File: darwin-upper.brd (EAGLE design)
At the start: 96 x 62 mm, 50 parts, among them U1 TC58CVG1S3HRAIG, U2 TC58CVG1S3HRAIG, U3 TC58CVG1S3HRAIG, U4 TC58CVG1S3HRAIG

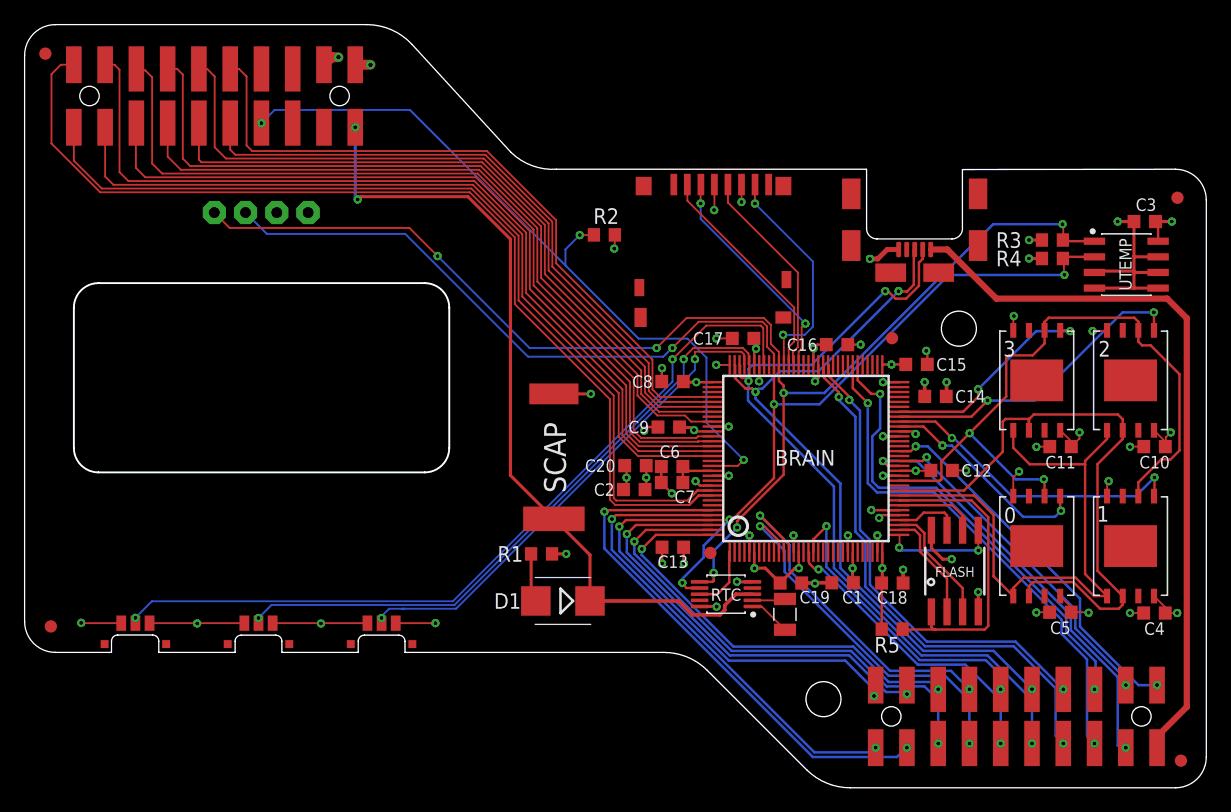
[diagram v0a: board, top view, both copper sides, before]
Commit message: Moved USB connector location, replaced buttons, tidied decoupling caps and routing.
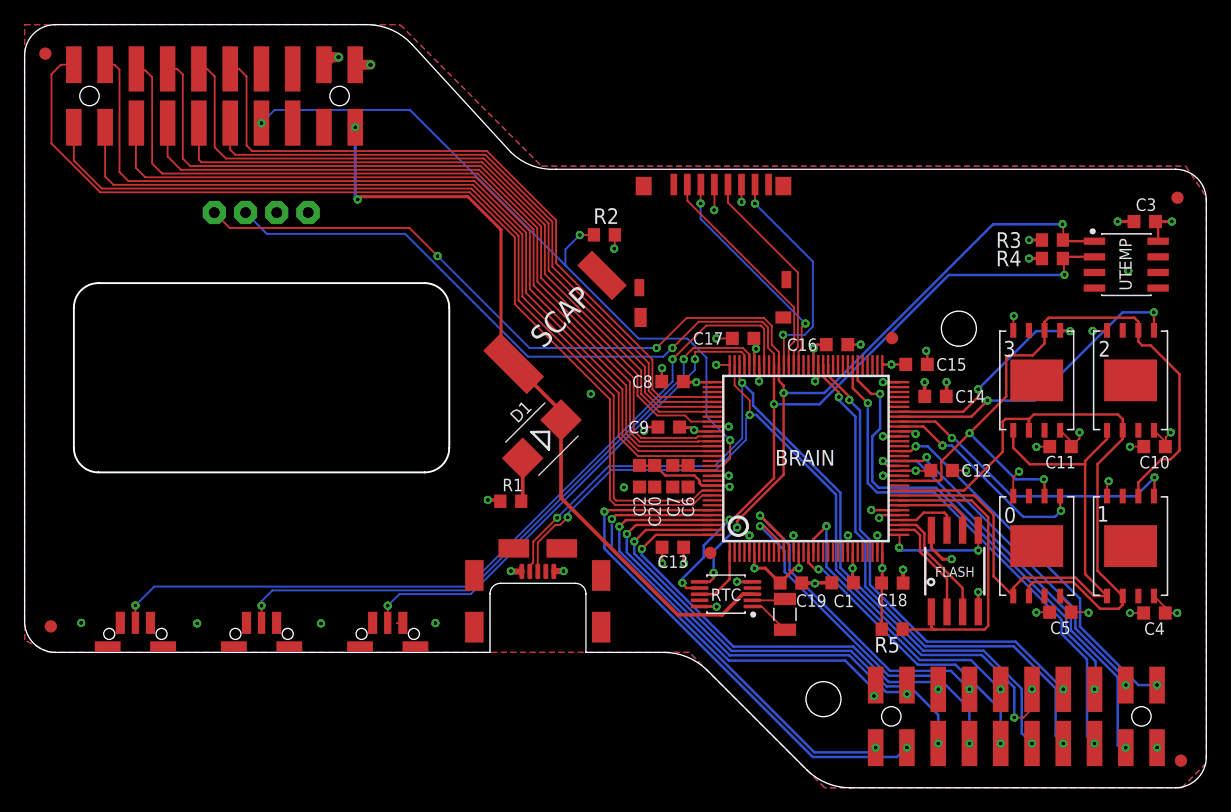
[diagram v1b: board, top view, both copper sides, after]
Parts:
- BTN1, BTN2, BTN3: value EVP-AEJB2A -> SKRTLAE010; device Conservify:EVP-AEJB2A -> Conservify:SKRTLAE010
- moved USB 41.4 mm to (44.7, 17.7), turned to 90 degrees
- moved D1 13.3 mm to (45.0, 29.3), turned to 225 degrees
- moved C23 11.1 mm to (46.4, 39.1), turned to 135 degrees
- moved R1 4.96 mm to (42.5, 24.3), turned to 0 degrees
- moved C20 1.78 mm to (54.2, 26.3), turned to 270 degrees
- moved BTN3 1.58 mm to (32.5, 13.5)
- moved BTN2 1.52 mm to (22.2, 13.5)
- moved C6 1.52 mm to (56.9, 26.3), turned to 270 degrees
- moved BTN1 1.50 mm to (12.0, 13.5)
- moved C2 1.17 mm to (53.0, 26.3), turned to 270 degrees
- moved C7 0.52 mm to (55.7, 26.3), turned to 270 degrees
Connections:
- net GND: now also BTN1.A, BTN1.A2, BTN1.TAB, BTN1.TAB2, BTN2.A, BTN2.A2, BTN2.TAB, BTN2.TAB2, BTN3.A, BTN3.A2, BTN3.TAB, BTN3.TAB2; no longer BTN1.A0, BTN1.A1, BTN2.A0, BTN2.A1, BTN3.A0, BTN3.A1
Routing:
- net GND: track 100.1 -> 51.6 mm
- net D+: track 59.4 -> 69.6 mm, vias 3 -> 4
- net D-: track 65.1 -> 71.0 mm
- net V5: track 59.0 -> 63.6 mm, vias 0 -> 2
- net 3V3: track 70.1 -> 73.8 mm, vias 29 -> 28
- net VBACKUP: track 66.6 -> 63.1 mm
- net RESET: track 61.3 -> 59.7 mm
- net MOD_G2: track 40.9 -> 40.2 mm
- net BUT1: track 65.3 -> 66.0 mm
- net SD_SCK: track 17.8 -> 17.2 mm
- net MOD_G7: track 24.8 -> 24.1 mm
- net BUT2: track 51.2 -> 51.8 mm
- added copper zone on layer 1, net GND
- added copper zone on layer 16, net GND
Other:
- outline, holes or cut-outs redrawn
- board text added: "BRAIN"
- board text added: "C1"
- board text added: "C10"
- board text added: "C11"
- board text added: "C12"
- board text added: "C13"
- board text added: "C14"
- board text added: "C15"
- board text added: "C16"
- board text added: "C17"
- board text added: "C18"
- board text added: "C19"
- board text added: "C2"
- board text added: "C20"
- board text added: "C3"
- board text added: "C4"
- board text added: "C5"
- board text added: "C6"
- board text added: "C7"
- board text added: "C8"
- board text added: "C9"
- board text added: "D1"
- board text added: "FLASH"
- board text added: "R1"
- board text added: "R2"
- board text added: "R3"
- board text added: "R4"
- board text added: "R5"
- board text added: "RTC"
- board text added: "SD"
- board text added: "UTEMP"

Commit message: Added Tag-Connect header.
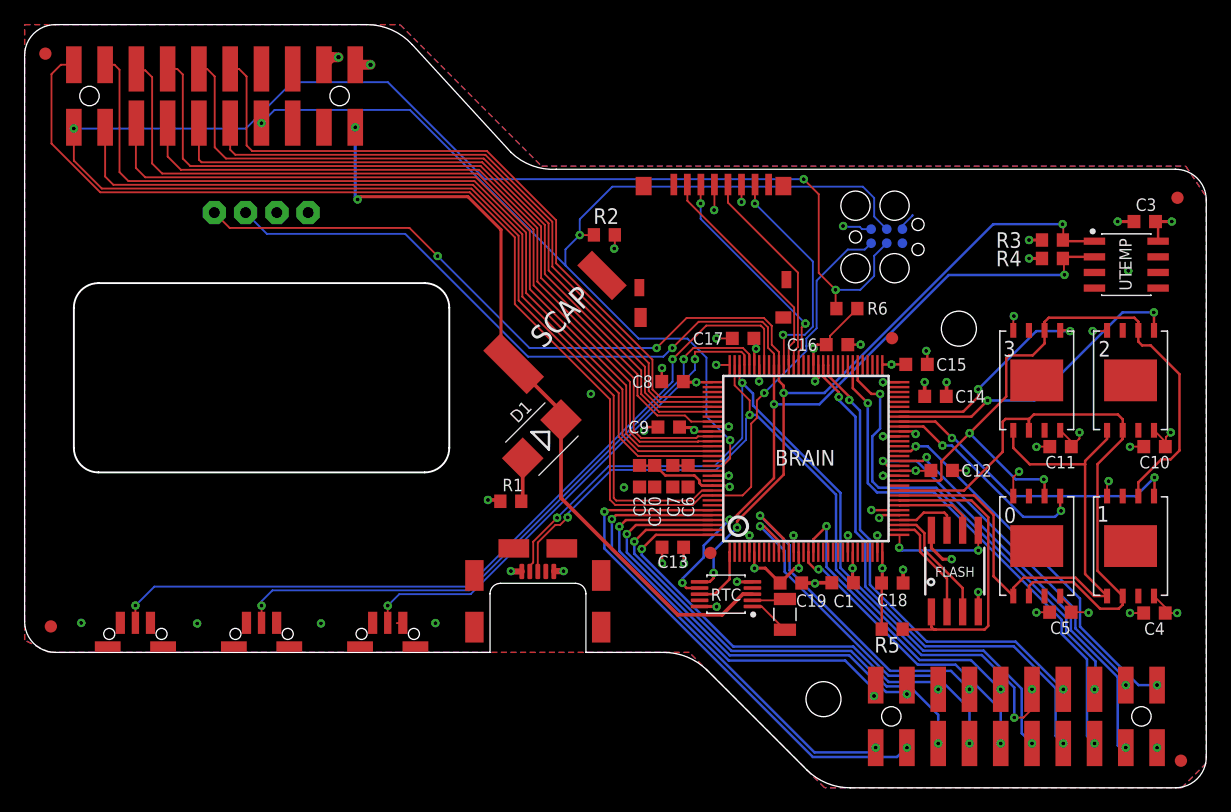
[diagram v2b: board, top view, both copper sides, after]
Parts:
- added J1: TAG-CONNECT, Conservify:TC2030-IDC
- added R6: 10k, rcl:R0603
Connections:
- new net SWO: J1.SWO/TDO
- net 3V3: now also J1.VCC, R6.2
- net GND: now also J1.GND
- net RESET: now also J1.NRESET
- net SWCLK: now also J1.SWCLK/TCK, R6.1
- net SWDIO: now also J1.SWDIO/TMS
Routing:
- net SWCLK: track 74.3 -> 156.7 mm, vias 0 -> 3
- net RESET: track 59.7 -> 89.3 mm
- net SWDIO: track 81.9 -> 110.0 mm, vias 0 -> 1
- net 3V3: track 73.8 -> 80.2 mm, vias 28 -> 29
- net GND: track 51.6 -> 53.1 mm

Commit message: Schematic cleanup and add PDF.
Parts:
- renumbered U$14 to XTAL
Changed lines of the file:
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@@
 <?xml version="1.0" encoding="utf-8"?>
 <!DOCTYPE eagle SYSTEM "eagle.dtd">
-<eagle version="9.5.2">
+<eagle version="9.6.1">
 <drawing>
 <settings>
@@
 <layer number="1" name="Top" color="4" fill="1" visible="yes" active="yes"/>
 <layer number="2" name="PWR" color="16" fill="1" visible="no" active="yes"/>
+<layer number="3" name="Route3" color="4" fill="3" visible="no" active="no"/>
+<layer number="4" name="Route4" color="1" fill="4" visible="no" active="no"/>
+<layer number="5" name="Route5" color="4" fill="4" visible="no" active="no"/>
+<layer number="6" name="Route6" color="1" fill="8" visible="no" active="no"/>
+<layer number="7" name="Route7" color="4" fill="8" visible="no" active="no"/>
+<layer number="8" name="Route8" color="1" fill="2" visible="no" active="no"/>
+<layer number="9" name="Route9" color="4" fill="2" visible="no" active="no"/>
+<layer number="10" name="Route10" color="1" fill="7" visible="no" active="no"/>
+<layer number="11" name="Route11" color="4" fill="7" visible="no" active="no"/>
+<layer number="12" name="Route12" color="1" fill="5" visible="no" active="no"/>
+<layer number="13" name="Route13" color="4" fill="5" visible="no" active="no"/>
+<layer number="14" name="Route14" color="1" fill="6" visible="no" active="no"/>
 <layer number="15" name="GND" color="23" fill="1" visible="no" active="yes"/>
 <layer number="16" name="Bottom" color="1" fill="1" visible="yes" active="yes"/>
@@
 <layer number="112" name="tSilk" color="7" fill="1" visible="yes" active="yes"/>
 <layer number="113" name="IDFDebug" color="4" fill="1" visible="yes" active="yes"/>
+<layer number="114" name="tPlaceRed" color="7" fill="1" visible="yes" active="yes"/>
+<layer number="115" name="FRNTMAAT2" color="7" fill="1" visible="yes" active="yes"/>
 <layer number="116" name="Patch_BOT" color="9" fill="4" visible="yes" active="yes"/>
+<layer number="117" name="BACKMAAT1" color="7" fill="1" visible="yes" active="yes"/>
 <layer number="118" name="Rect_Pads" color="7" fill="1" visible="yes" active="yes"/>
+<layer number="119" name="KAP_TEKEN" color="7" fill="1" visible="yes" active="yes"/>
+<layer number="120" name="KAP_MAAT1" color="7" fill="1" visible="yes" active="yes"/>
 <layer number="121" name="_tsilk" color="7" fill="1" visible="yes" active="yes"/>
 <layer number="122" name="_bsilk" color="7" fill="1" visible="yes" active="yes"/>
@@
 <layer number="128" name="_bValues" color="7" fill="1" visible="yes" active="yes"/>
 <layer number="129" name="Mask" color="7" fill="1" visible="yes" active="yes"/>
+<layer number="130" name="SMDSTROOK" color="7" fill="1" visible="yes" active="yes"/>
 <layer number="131" name="tAdjust" color="7" fill="1" visible="yes" active="yes"/>
 <layer number="132" name="bAdjust" color="7" fill="1" visible="yes" active="yes"/>
+<layer number="133" name="bottom_silk" color="7" fill="1" visible="yes" active="yes"/>
 <layer number="144" name="Drill_legend" color="7" fill="1" visible="yes" active="yes"/>
 <layer number="150" name="Notes" color="7" fill="1" visible="yes" active="yes"/>
@@
 <layer number="230" name="230bmp" color="7" fill="1" visible="yes" active="yes"/>
 <layer number="231" name="231bmp" color="7" fill="1" visible="yes" active="yes"/>
+<layer number="232" name="Eagle3D_PG2" color="7" fill="1" visible="yes" active="yes"/>
+<layer number="233" name="Eagle3D_PG3" color="7" fill="1" visible="yes" active="yes"/>
 <layer number="248" name="Housing" color="7" fill="1" visible="yes" active="yes"/>
 <layer number="249" name="Edge" color="7" fill="1" visible="yes" active="yes"/>
@@
 </layers>
 <board>
-<fusionsync huburn="a.cGVyc29uYWw6dWUyZGRkM2Mx" projecturn="a.cGVyc29uYWw6dWUyZGRkM2MxIzIwMTgwNTA0MTMwNDQ3NTc2" f3durn="urn:adsk.wipprod:dm.lineage:B8w4oF1WQnCwF1kTAVzY8Q" pcbguid="5f6603c8-1044-428d-87b9-4eb708af9043" lastpulledtime="" lastsyncedchangeguid="898615ed-fd74-069b-006d-062865fd968c"/>
+<fusionsync huburn="a.cGVyc29uYWw6dWUyZGRkM2Mx" projecturn="a.cGVyc29uYWw6dWUyZGRkM2MxIzIwMTgwNTA0MTMwNDQ3NTc2" f3durn="urn:adsk.wipprod:dm.lineage:B8w4oF1WQnCwF1kTAVzY8Q" pcbguid="5f6603c8-1044-428d-87b9-4eb708af9043" lastpulledtime="" lastsyncedchangeguid="898615ed-fd74-069b-006d-062865fd968c" latestrevisionid="" lastsyncedrevisionid="" lastboardhashguid="" lastpushedtime="" linktopcb3d="%12"/>
 <plain>
 <wire x1="3" y1="60.5" x2="3" y2="14.5" width="0" layer="20"/>
@@
 <element name="BTN2" library="Conservify" library_urn="urn:adsk.eagle:library:11839183" package="SKRTLAE010" package3d_urn="urn:adsk.eagle:package:15671107/2" value="SKRTLAE010" x="22.25" y="13.5" smashed="yes"/>
 <element name="BTN3" library="Conservify" library_urn="urn:adsk.eagle:library:11839183" package="SKRTLAE010" package3d_urn="urn:adsk.eagle:package:15671107/2" value="SKRTLAE010" x="32.5" y="13.5" smashed="yes"/>
-<element name="U$14" library="Conservify" library_urn="urn:adsk.eagle:library:11839183" package="ABS07W" package3d_urn="urn:adsk.eagle:package:11839243/1" value="ABS07W" x="64.77" y="15.0876" smashed="yes" rot="R270"/>
+<element name="XTAL" library="Conservify" library_urn="urn:adsk.eagle:library:11839183" package="ABS07W" package3d_urn="urn:adsk.eagle:package:11839243/1" value="ABS07W" x="64.77" y="15.0876" smashed="yes" rot="R270"/>
 <element name="UTEMP" library="Conservify" library_urn="urn:adsk.eagle:library:11839183" package="SO8" package3d_urn="urn:adsk.eagle:package:11214694/2" value="PCT2075" x="92.5" y="43.5" smashed="yes">
 <attribute name="NAME" x="92.9335" y="43.518" size="1" layer="25" rot="R90" align="bottom-center"/>
@@
 <wire x1="68.4298" y1="37.7094" x2="68.4298" y2="37.3048" width="0.1524" layer="1"/>
 <wire x1="68.4298" y1="37.3048" x2="68.125" y2="37" width="0.1524" layer="1"/>
+<wire x1="85.65" y1="45.5" x2="94.875" y2="47" width="0" layer="19" extent="1-1"/>
+<wire x1="84.582" y1="44.0436" x2="84.582" y2="45.4152" width="0" layer="19" extent="2-2"/>
+<wire x1="71.77" y1="46.385" x2="84.582" y2="45.4152" width="0" layer="19" extent="2-16"/>
+<wire x1="70.6492" y1="39.9288" x2="71.77" y2="46.385" width="0" layer="19" extent="1-16"/>
+<wire x1="62.4222" y1="36.6684" x2="67.0896" y2="36.6908" width="0" layer="19" extent="1-1"/>
+<wire x1="58.88" y1="33.95" x2="62.28" y2="35.35" width="0" layer="19" extent="1-1"/>
+<wire x1="56.2052" y1="30.3048" x2="56.51" y2="34" width="0" layer="19" extent="1-1"/>
+<wire x1="54.188" y1="27.1876" x2="56.2052" y2="30.3048" width="0" layer="19" extent="1-1"/>
+<wire x1="72.68" y1="35.35" x2="68.125" y2="37" width="0" layer="19" extent="1-1"/>
+<wire x1="76.121" y1="33.955" x2="74.585" y2="35.397" width="0" layer="19" extent="1-1"/>
+<wire x1="75.3856" y1="29.7428" x2="76.125" y2="32.8" width="0" layer="19" extent="1-1"/>
+<wire x1="75.3954" y1="26.7594" x2="75.3856" y2="29.7428" width="0" layer="19" extent="1-1"/>
+<wire x1="74.08" y1="23.15" x2="74.08" y2="26.75" width="0" layer="19" extent="1-1"/>
+<wire x1="72.68" y1="20.15" x2="72.4236" y2="22.924" width="0" layer="19" extent="1-1"/>
+<wire x1="70.3302" y1="17.6556" x2="72.617" y2="17.635" width="0" layer="19" extent="1-1"/>
+<wire x1="76.6654" y1="21.921" x2="74.08" y2="23.15" width="0" layer="19" extent="1-1"/>
+<wire x1="65.8958" y1="18.8346" x2="70.2646" y2="18.8346" width="0" layer="19" extent="1-1"/>
+<wire x1="59.219" y1="15.712" x2="62.289" y2="18.8346" width="0" layer="19" extent="1-1"/>
+<wire x1="56.563" y1="19.223" x2="57.8356" y2="15.728" width="0" layer="19" extent="1-1"/>
+<wire x1="87.1302" y1="16.578" x2="78.3164" y2="19.5712" width="0" layer="19" extent="1-1"/>
+<wire x1="94.7502" y1="16.578" x2="89.4588" y2="15.24" width="0" layer="19" extent="1-2"/>
+<wire x1="59.0169" y1="47.9298" x2="69.4944" y2="46.6344" width="0" layer="19" extent="1-1"/>
+<wire x1="50.9484" y1="45.9188" x2="59.0169" y2="47.9298" width="0" layer="19" extent="1-1"/>
+<wire x1="87.1302" y1="30.04" x2="76.6264" y2="26.7808" width="0" layer="19" extent="1-1"/>
+<wire x1="94.7502" y1="30.04" x2="88.6968" y2="29.8704" width="0" layer="19" extent="1-1"/>
+<wire x1="41.646" y1="24.276" x2="52.957" y2="27.1892" width="0" layer="19" extent="1-1"/>
+<wire x1="26.03" y1="47.73" x2="50.9484" y2="45.9188" width="0" layer="19" extent="1-1"/>
+<wire x1="27.32" y1="59.74" x2="26.03" y2="47.73" width="0" layer="19" extent="1-1"/>
 </signal>
 <signal name="GND">
@@
 <signal name="N$3">
 <contactref element="RTC" pad="1"/>
-<contactref element="U$14" pad="P$2"/>
+<contactref element="XTAL" pad="P$2"/>
 <wire x1="62.1264" y1="15.728" x2="62.8796" y2="15.728" width="0.1524" layer="1"/>
 <wire x1="62.8796" y1="15.728" x2="64.77" y2="13.8376" width="0.1524" layer="1"/>
@@
 <signal name="N$4">
 <contactref element="RTC" pad="2"/>
-<contactref element="U$14" pad="P$1"/>
+<contactref element="XTAL" pad="P$1"/>
 <wire x1="64.6604" y1="16.228" x2="64.77" y2="16.3376" width="0.1524" layer="1"/>
 <wire x1="62.1264" y1="16.228" x2="64.6604" y2="16.228" width="0.1524" layer="1"/>
